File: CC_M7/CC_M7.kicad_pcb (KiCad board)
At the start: 4 copper layers, 40 x 65 mm, 129 parts, among them J1 Conn_01x04_Pin, J10 Conn_01x04_Pin, J11 USB_B_Micro, J12 Conn_01x04_Pin, J13 Batt_Pins, J3 Conn_01x03_Pin, J4 Conn_01x03_Pin, J5 Conn_01x03_Pin, J6 Conn_01x03_Pin, J7 Conn_01x03_Pin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

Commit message: warning check
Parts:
- H1, H2, H3, H4, H5, H6: footprint MountingHole:MountingHole_3.2mm_M3_ISO14580_Pad -> MountingHole:CCMountingHole
- JP1, JP2, JP3, JP4, JP5, JP6, JP7, JP8: footprint Jumper:SolderJumper-2_P1.3mm_Open_TrianglePad1.0x1.5mm -> jmpertest:jmpertest; moved to F.Cu
- moved H2 69.0 mm to (114.1, 108.8)
- moved H1 65.0 mm to (124.1, 108.8)
- moved H6 52.0 mm to (124.1, 166.8)
- moved H5 52.0 mm to (114.1, 166.8)
- moved H4 23.9 mm to (91.1, 166.8)
- moved H3 6.96 mm to (91.1, 108.8)
- moved JP7 0.55 mm to (99.4, 121.9)
- moved JP1 0.55 mm to (96.9, 122.6)
- moved JP8 0.54 mm to (99.4, 121.0)
- moved JP3 0.52 mm to (96.9, 120.8)
- moved JP6 0.50 mm to (99.3, 122.8)
- moved JP4 0.47 mm to (96.9, 120.0)
- moved JP5 0.47 mm to (99.3, 123.6)
- moved JP2 0.46 mm to (96.9, 121.8)

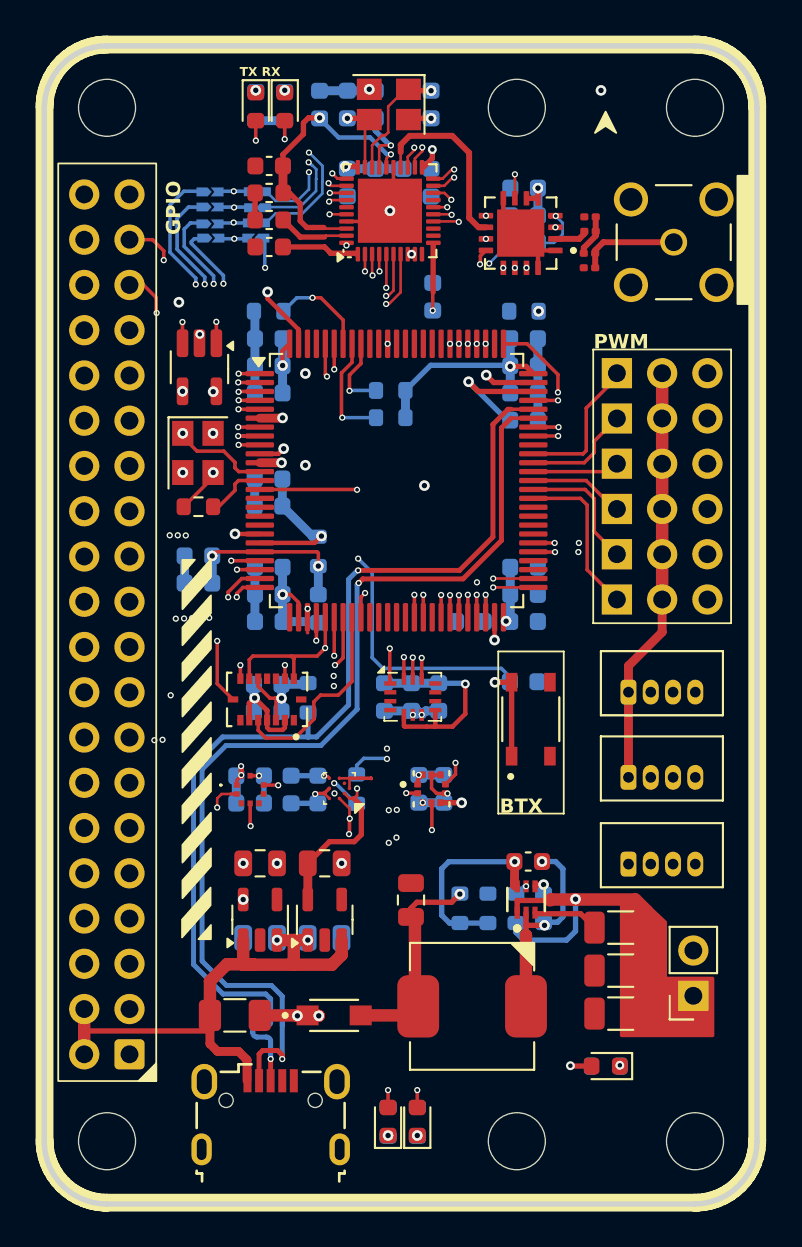
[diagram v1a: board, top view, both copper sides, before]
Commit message: Zones properties changed.
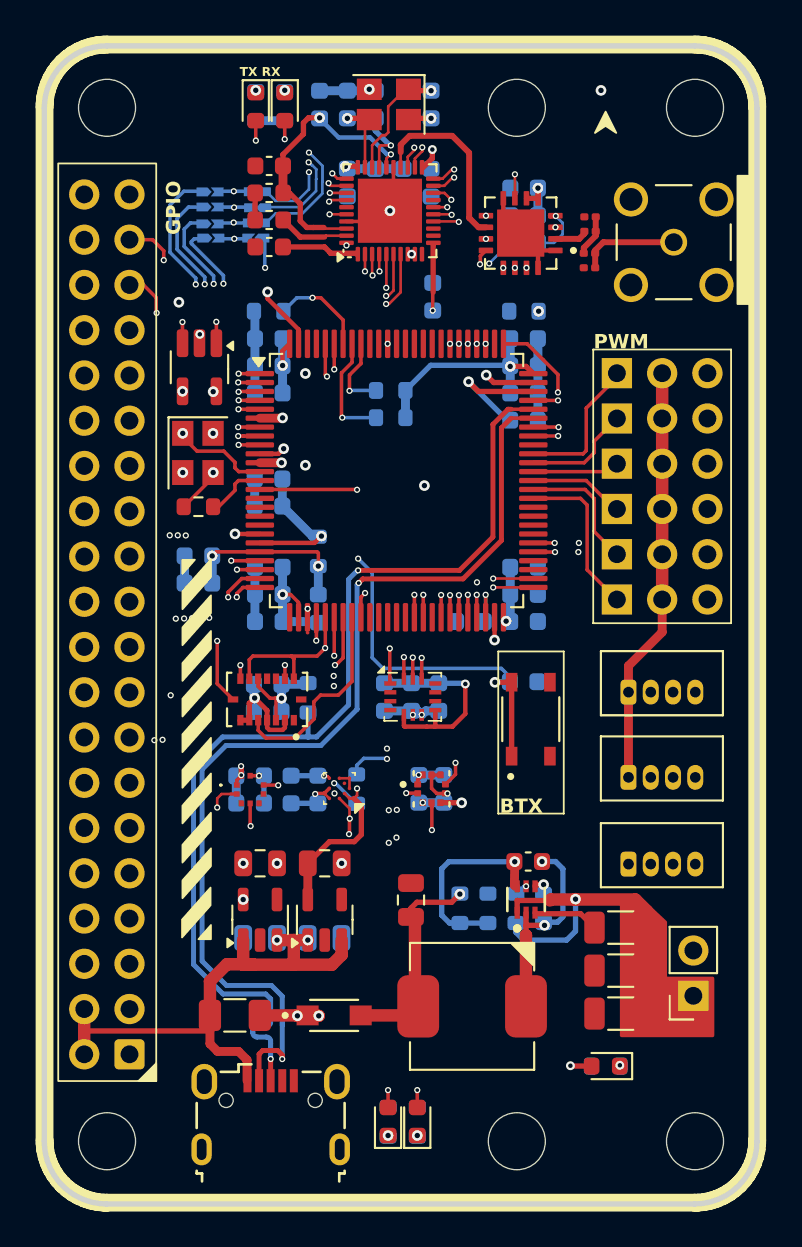
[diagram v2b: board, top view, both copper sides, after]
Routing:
- net +3.3V: track 66.1 -> 67.7 mm
- added copper zone on B.Cu, net +3.3V
- added copper zone on F.Cu, net +3.3V
- added copper zone on In1.Cu, net +3.3V
- removed copper zone on B.Cu, net GND
- removed copper zone on In1.Cu, net GND
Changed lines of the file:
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@@
 	)
 	(segment
-		(start 105.85 153.43)
-		(end 105.837 153.417)
-		(width 0.2)
-		(layer "F.Cu")
-		(net 1)
-	)
-	(segment
 		(start 102.73 154.27)
 		(end 102.72 154.28)
@@
 	)
 	(segment
-		(start 105.84 153.42)
-		(end 105.84 153.42)
-		(width 0.2)
-		(layer "F.Cu")
-		(net 1)
-	)
-	(segment
 		(start 103.492 154.549)
 		(end 103.2215 154.2785)
@@
 	)
 	(segment
-		(start 105.837 153.417)
-		(end 104.624 153.417)
-		(width 0.2)
-		(layer "F.Cu")
-		(net 1)
-	)
-	(segment
 		(start 100.93 134.92)
 		(end 100.643 135.207)
@@
 	)
 	(segment
-		(start 105.84 153.42)
-		(end 105.85 153.43)
-		(width 0.2)
-		(layer "F.Cu")
-		(net 1)
-	)
-	(segment
 		(start 106.294567 122.1653)
 		(end 106.894567 121.5653)
@@
 	)
 	(segment
+		(start 98.5012 150.158)
+		(end 99.0012 150.158)
+		(width 0.3)
+		(layer "F.Cu")
+		(net 1)
+	)
+	(segment
 		(start 98.48 150.1792)
 		(end 98.5012 150.158)
@@
 	)
 	(segment
+		(start 113.652 121.8408)
+		(end 113.1408 121.8408)
+		(width 0.3)
+		(layer "B.Cu")
+		(net 1)
+	)
+	(segment
 		(start 108.74 154.786)
 		(end 108.52 154.786)
@@
 	)
 	(segment
+		(start 92.31 148.59)
+		(end 93.4 147.5)
+		(width 0.3)
+		(layer "In2.Cu")
+		(net 2)
+	)
+	(segment
+		(start 92.2782 148.59)
+		(end 92.31 148.59)
+		(width 0.3)
+		(layer "In2.Cu")
+		(net 2)
+	)
+	(segment
 		(start 100.870192 131.793876)
 		(end 100.870192 130.2512)
@@
 		(net 1)
 		(net_name "GND")
-		(layers "F.Cu" "In1.Cu" "B.Cu")
+		(layer "F.Cu")
 		(hatch edge 0.5)
 		(connect_pads
@@
 		(filled_areas_thickness no)
 		(fill yes
-			(thermal_gap 0.3)
-			(thermal_bridge_width 0.2)
-			(island_removal_mode 1)
-			(island_area_min 10)
+			(thermal_gap 0.4)
+			(thermal_bridge_width 0.25)
 		)
 		(polygon
@@
 		(net 2)
 		(net_name "+3.3V")
-		(layer "In2.Cu")
+		(layers "F.Cu" "In1.Cu" "In2.Cu" "B.Cu")
 		(hatch edge 0.5)
-		(connect_pads
+		(connect_pads yes
 			(clearance 0.3)
 		)
@@
 		(filled_areas_thickness no)
 		(fill yes
-			(thermal_gap 0.3)
-			(thermal_bridge_width 0.2)
-			(island_removal_mode 1)
-			(island_area_min 10)
+			(thermal_gap 0.4)
+			(thermal_bridge_width 0.25)
 		)
 		(polygon

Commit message: Error and warning completed check.
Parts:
- turned R13 to -90 degrees
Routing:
- net GND: track 67.1 -> 178.1 mm, vias 25 -> 28
- net +3.3V: track 67.7 -> 78.0 mm, vias 16 -> 17
- net Net-(U8-FB): track 11.1 -> 6.14 mm
- net Net-(C18-Pad1): track 7.09 -> 7.70 mm
- added copper zone on B.Cu, net GND
- added copper zone on In2.Cu, net GND
- removed copper zone on B.Cu, net +3.3V
- removed copper zone on F.Cu, net +3.3V
- removed copper zone on In1.Cu, net +3.3V

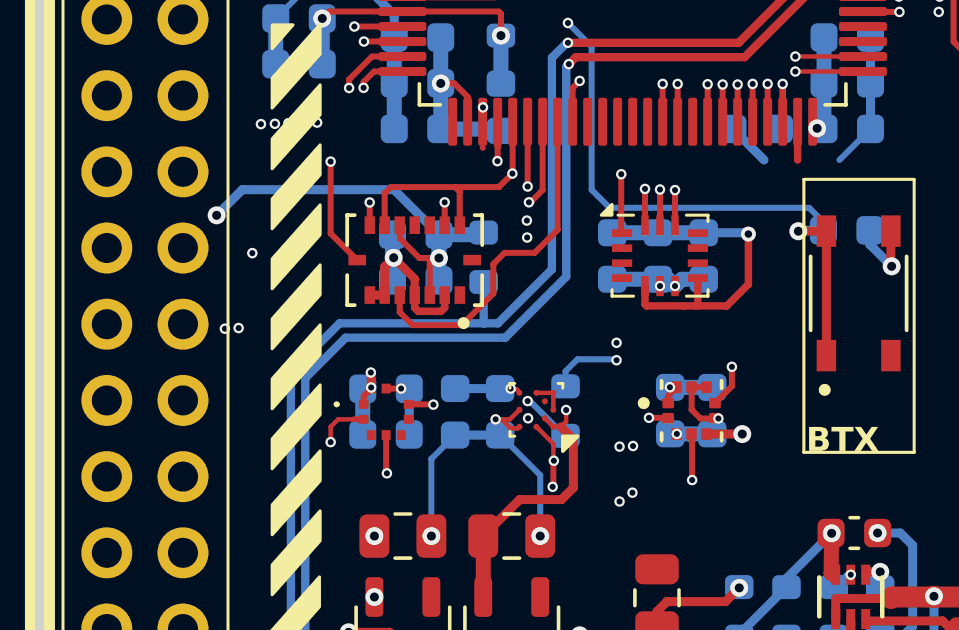
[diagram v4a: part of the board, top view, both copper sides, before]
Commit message: Adding 3d models.
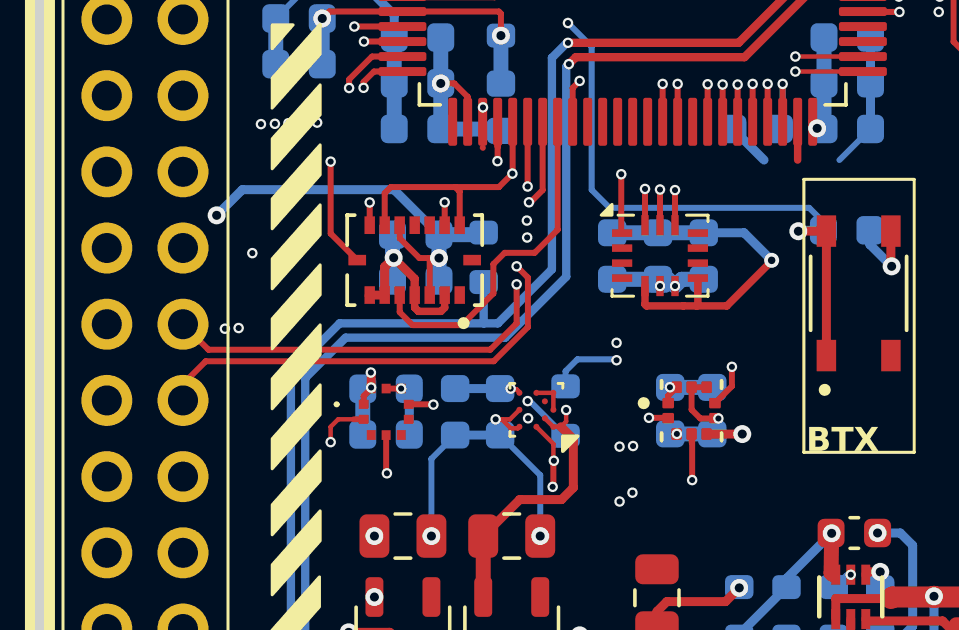
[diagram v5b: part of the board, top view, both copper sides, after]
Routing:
- net CAN2_RX: track 2.25 -> 31.5 mm, vias 1 -> 2
- net CAN2_TX: track 2.25 -> 31.1 mm, vias 1 -> 2
- net I2C1_IRQ1: track 20.8 -> 20.0 mm
- net +3.3V: track 78.0 -> 78.6 mm
